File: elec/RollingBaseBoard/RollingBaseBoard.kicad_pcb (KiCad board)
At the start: 2 copper layers, 80 x 80 mm, 102 parts, among them P1 GP2, P10 UART_2, P11 I2C, P12 Motor, P13 Motor, P14 Encoder2, P15 Motor, P16 Switch, P17 Switch, P18 Switch, P19 Switch, P2 GP2, P20 Switch, P3 GP2, P4 GP2, P5 Bat5V, P6 Bat15V, P7 Encoder, P8 Encoder, P9 UART_1, U1 LMD18201, U2 LMD18201, U3 Teensy3.1

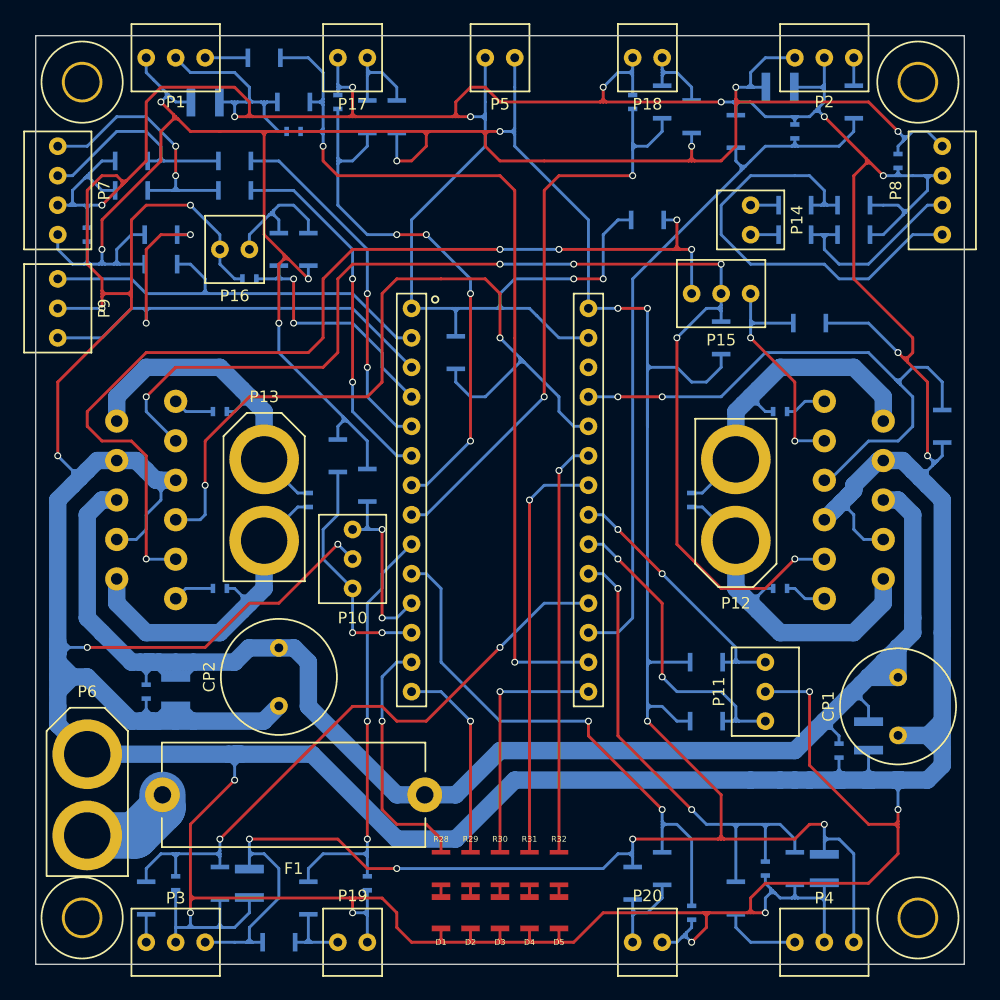
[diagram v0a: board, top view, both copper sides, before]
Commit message: Fixing rolling base board routing after footprints change.
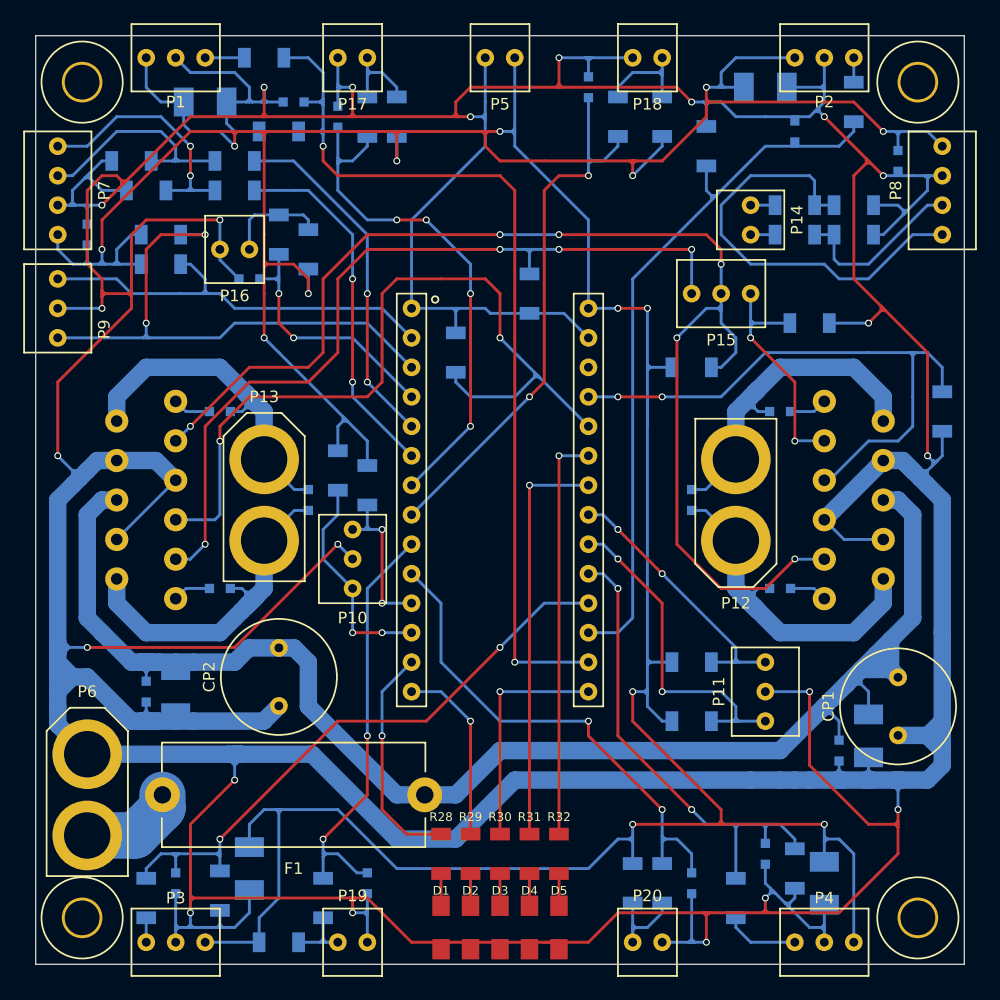
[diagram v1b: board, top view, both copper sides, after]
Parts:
- moved R26 12.0 mm to (151.0, 87.2), turned to 90 degrees
- moved R38 4.02 mm to (158.7, 72.0)
- moved C23 4.02 mm to (156.1, 69.4)
- moved R1 3.59 mm to (165.0, 93.6), turned to 180 degrees
- moved R3 2.84 mm to (129.4, 73.2)
- moved R5 2.84 mm to (166.3, 74.5)
- moved C2 2.54 mm to (130.7, 70.7)
- moved C25 2.54 mm to (165.0, 138.0)
- moved R37 2.54 mm to (162.5, 72.0)
- moved C22 1.27 mm to (134.5, 72.0)
- moved C5 1.27 mm to (126.9, 136.8)
- moved C7 1.27 mm to (176.4, 138.0)
- moved C8 1.27 mm to (171.4, 135.5)
- moved D1 1.27 mm to (143.4, 141.8)
- moved D2 1.27 mm to (146.0, 141.8)
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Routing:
- net /Com/GND: track 795.0 -> 745.9 mm, vias 24 -> 22
- net /Driver_2/Direction: track 87.9 -> 71.8 mm, vias 5 -> 4
- net /Driver_1/+15V: track 151.3 -> 137.2 mm
- net /Com/+5V: track 372.5 -> 378.7 mm, vias 16 -> 14
- net Net-(C18-Pad1): track 31.6 -> 35.7 mm
- net Net-(C18-Pad2): track 32.4 -> 36.5 mm
- net /Teensy/LimitSwitch2: track 52.2 -> 48.4 mm
- net /Teensy/LimitSwitch4: track 47.7 -> 43.8 mm
- net /Driver_1/ThermalFlag: track 106.5 -> 109.6 mm
- net Net-(P16-Pad2): track 11.9 -> 8.82 mm
- net Net-(C13-Pad1): track 31.6 -> 34.1 mm
- net /Teensy/LimitSwitch1: track 47.9 -> 45.5 mm
- net Net-(R28-Pad1): track 21.8 -> 19.7 mm
- net /Com/SDA: track 27.9 -> 29.8 mm
- net Net-(P18-Pad2): track 7.33 -> 9.27 mm
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
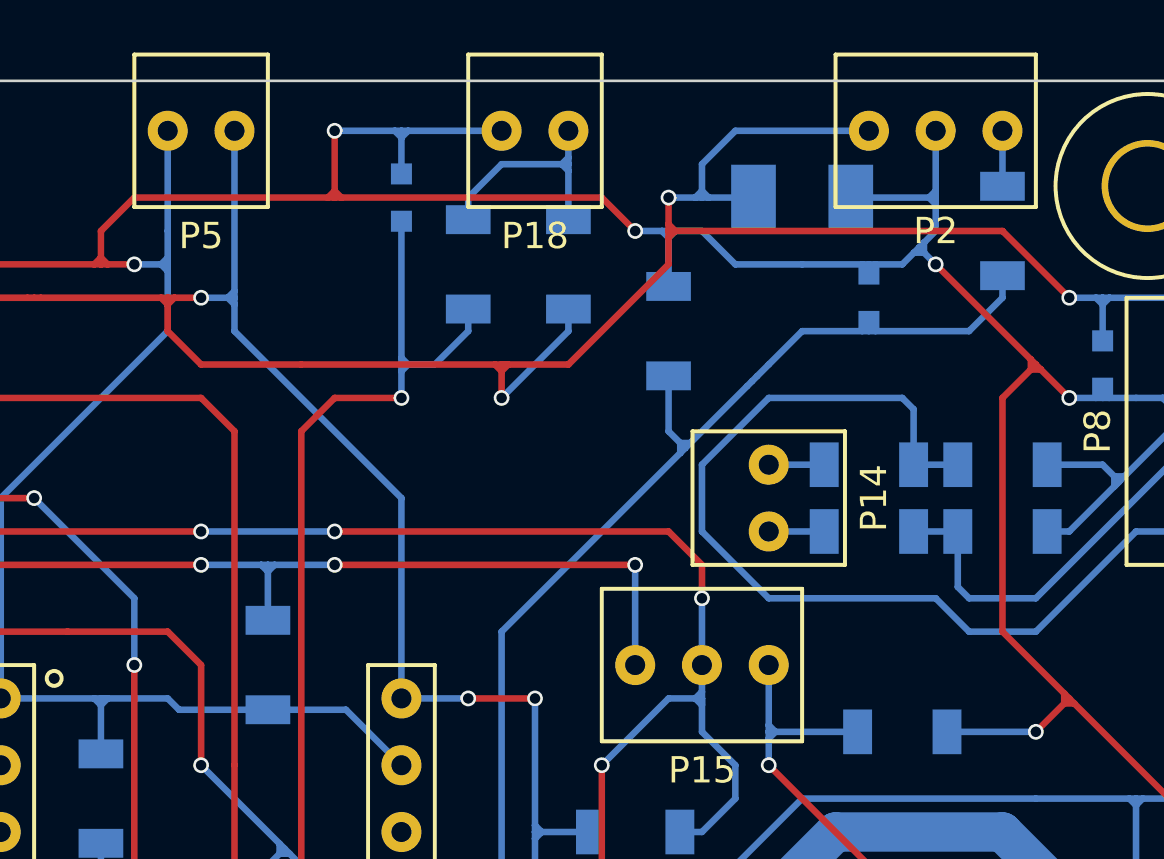
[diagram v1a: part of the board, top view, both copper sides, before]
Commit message: Optimising rolling base board routing a bit
Reduced via count by 6
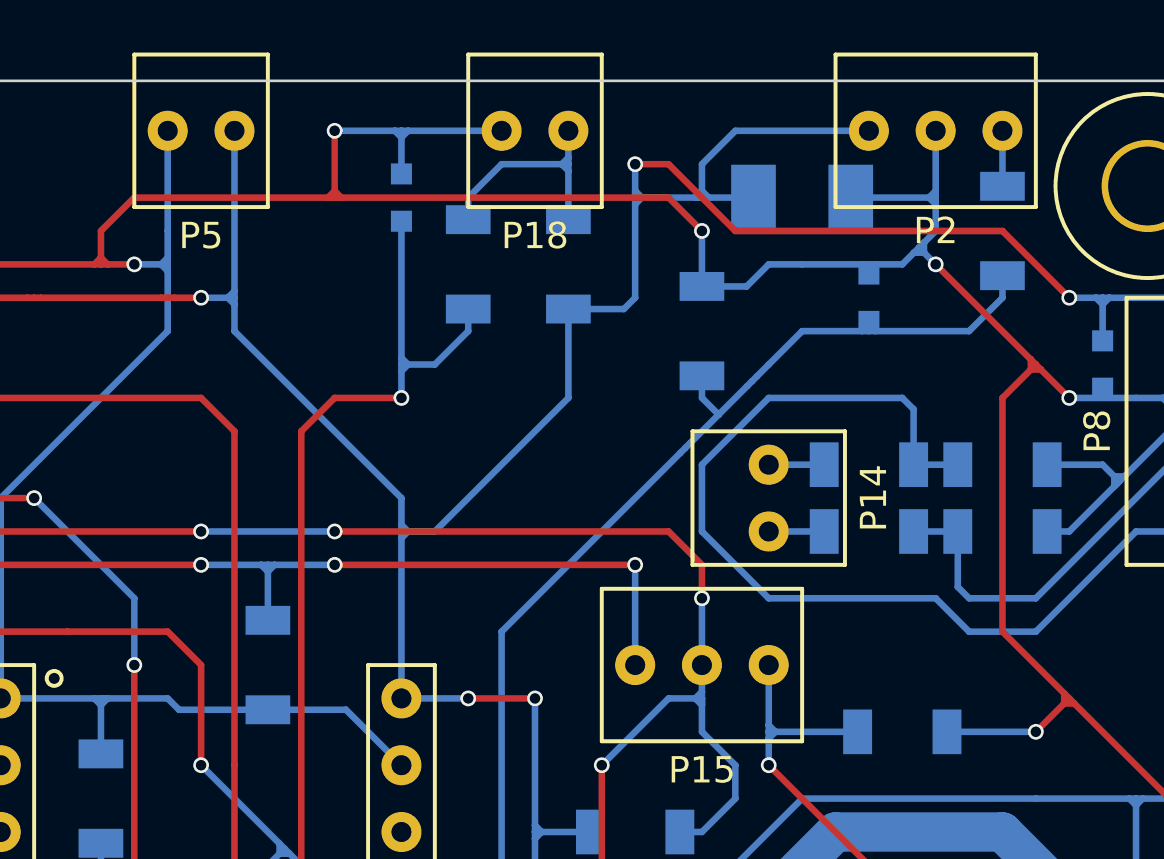
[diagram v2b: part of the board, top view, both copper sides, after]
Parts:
- moved R5 1.27 mm to (167.6, 74.5)
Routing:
- net /Com/+5V: track 378.7 -> 370.5 mm, vias 14 -> 13
- net /Teensy/GP2_2: track 62.5 -> 60.4 mm
- net /Com/GND: track 745.9 -> 744.7 mm

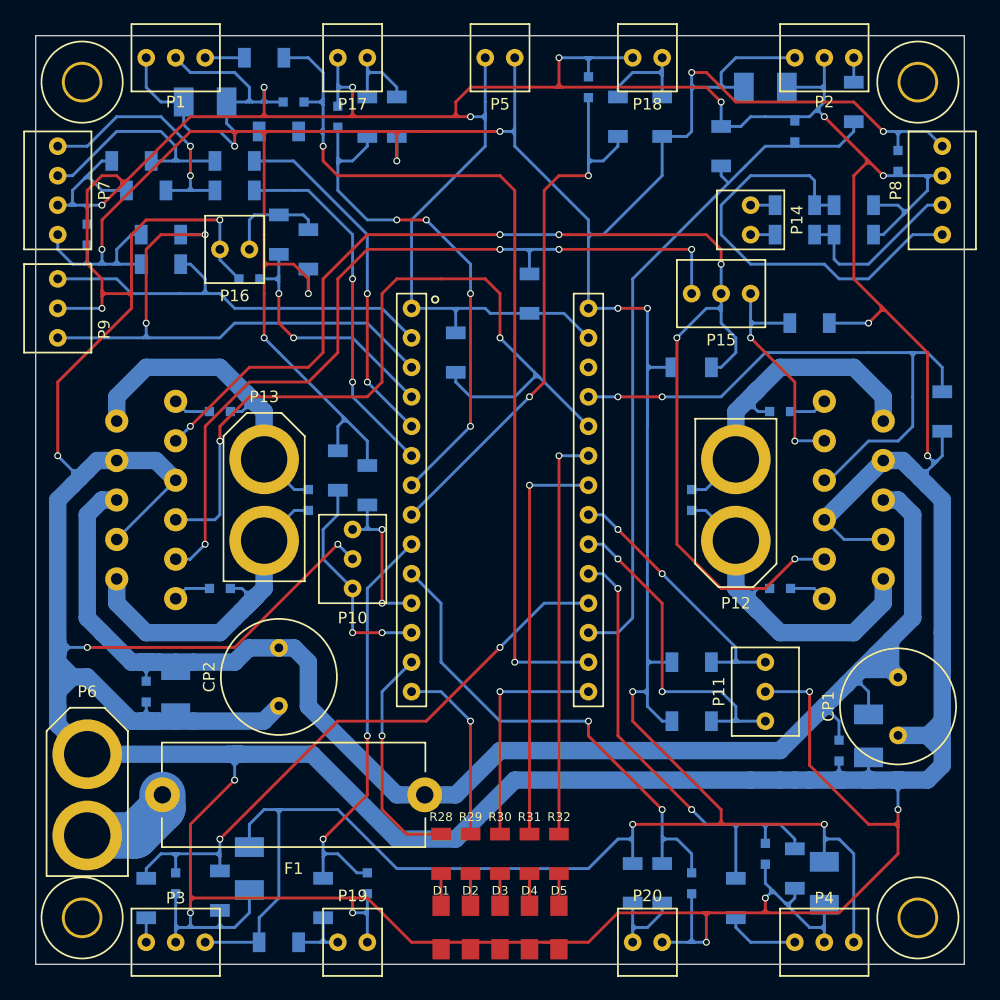
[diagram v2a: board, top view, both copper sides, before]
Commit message: Optimising rolling base board routing some more. Also removing a GND loop.
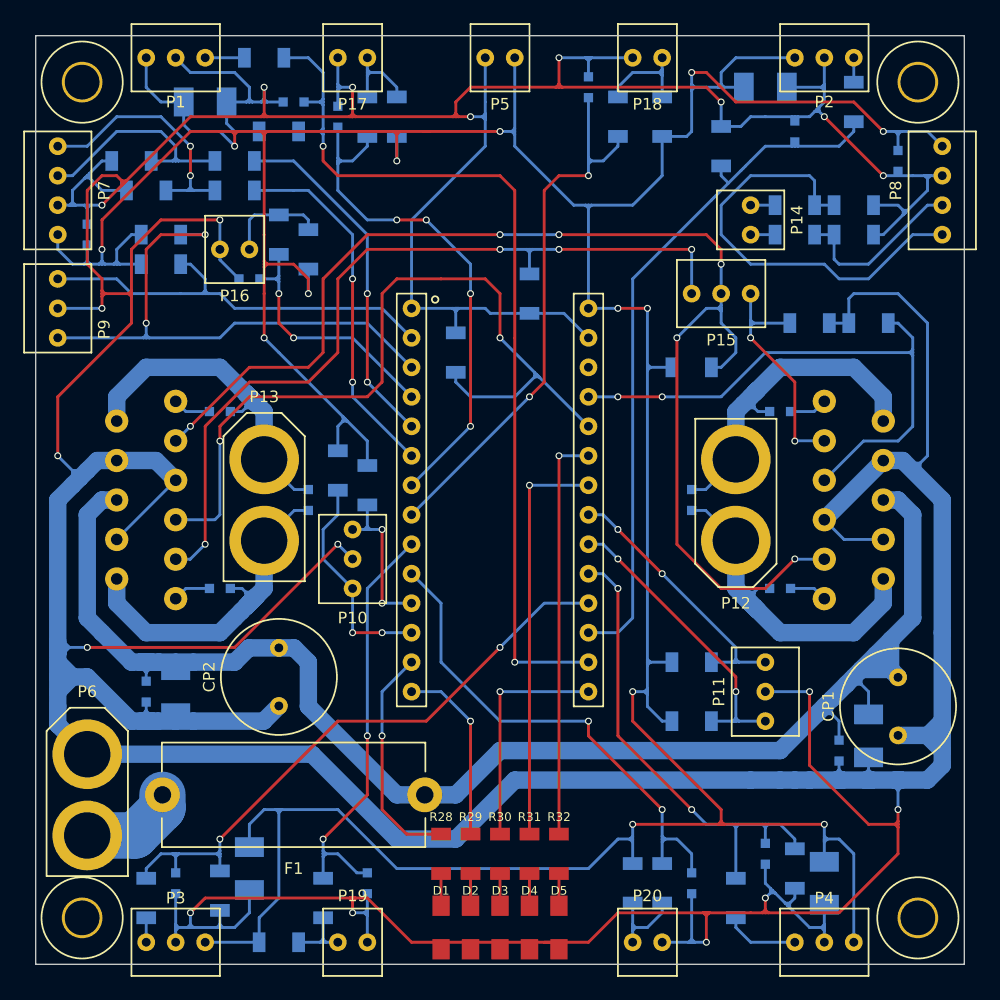
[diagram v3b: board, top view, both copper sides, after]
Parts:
- moved R25 9.92 mm to (180.2, 89.8), turned to 0 degrees
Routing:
- net /Com/GND: track 744.7 -> 708.7 mm, vias 22 -> 19
- net /Com/SDA: track 29.8 -> 27.1 mm
- net (no net): track 2.54 -> 0.00 mm
- net /Driver_1/PWM: track 51.3 -> 50.0 mm

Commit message: The rolling base board now has a name. Please welcome Hermes in the family.
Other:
- board text added: "Hermes board v1 Xenomorphales"
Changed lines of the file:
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@@
     (area 105.275 61.775 191.575 148.075)
     (thickness 1.6)
-    (drawings 4)
+    (drawings 5)
     (tracks 1367)
     (zones 0)
@@
       (net 2 /Com/+5V))
   )
+  (gr_text "Hermes board v1\n\nXenomorphales" (at 148.5 77.06) (layer F.SilkS)
+    (effects (font (size 1.5 1.5) (thickness 0.3)))
+  )
   (gr_line (start 108.5 145) (end 108.5 65) (angle 90) (layer Edge.Cuts) (width 0.1))

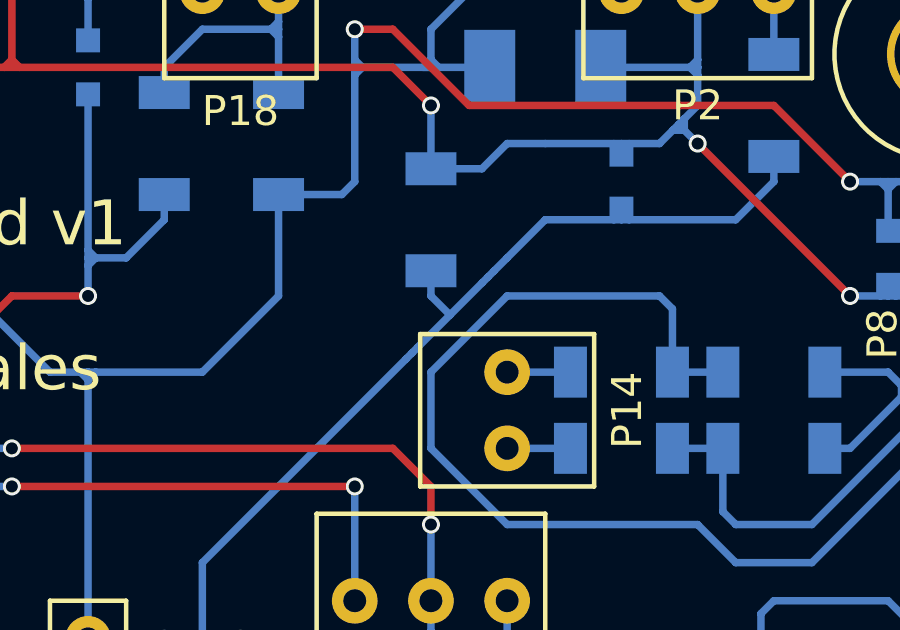
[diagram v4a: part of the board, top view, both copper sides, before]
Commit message: Minor fix to rolling base board routing
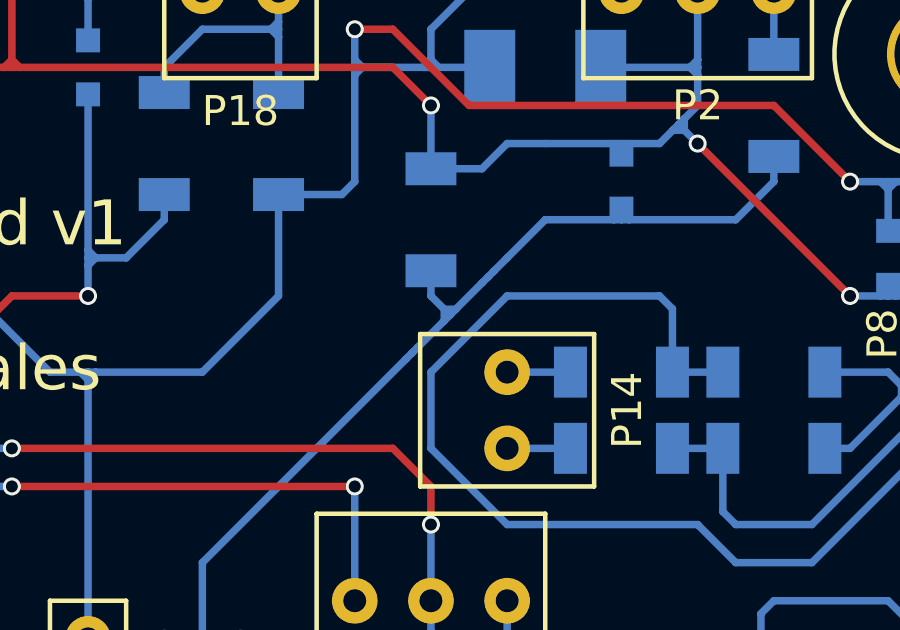
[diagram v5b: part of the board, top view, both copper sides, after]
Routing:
- net /Teensy/GP2_2: track 60.4 -> 61.2 mm
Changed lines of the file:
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@@
     (thickness 1.6)
     (drawings 5)
-    (tracks 1367)
+    (tracks 1372)
     (zones 0)
     (modules 102)
@@
   (segment (start 133.26 70.456) (end 133.26 70.71) (width 0.25) (layer B.Cu) (net 3))
   (segment (start 133.26 70.71) (end 133.26 70.964) (width 0.25) (layer B.Cu) (net 3))
+  (segment (start 167.9945 77.5045) (end 168.3755 77.5045) (width 0.25) (layer B.Cu) (net 4))
+  (segment (start 167.9945 77.5045) (end 167.9945 77.8855) (width 0.25) (layer B.Cu) (net 4))
   (segment (start 167.55 76.22) (end 167.55 77.06) (width 0.25) (layer B.Cu) (net 4))
-  (segment (start 167.55 77.06) (end 168.185 77.695) (width 0.25) (layer B.Cu) (net 4))
+  (segment (start 167.55 77.06) (end 167.9945 77.5045) (width 0.25) (layer B.Cu) (net 4))
+  (segment (start 167.9945 77.5045) (end 168.185 77.695) (width 0.25) (layer B.Cu) (net 4))
   (segment (start 178.98 72.41) (end 178.98 73.25) (width 0.25) (layer B.Cu) (net 4))
   (segment (start 177.71 74.52) (end 174.154 74.52) (width 0.25) (layer B.Cu) (net 4))
   (segment (start 178.98 73.25) (end 177.71 74.52) (width 0.25) (layer B.Cu) (net 4))
   (segment (start 169.455 76.425) (end 169.2645 76.6155) (width 0.25) (layer B.Cu) (net 4))
+  (segment (start 169.2645 76.6155) (end 168.3755 77.5045) (width 0.25) (layer B.Cu) (net 4))
+  (segment (start 169.455 76.425) (end 169.6455 76.2345) (width 0.25) (layer B.Cu) (net 4))
+  (segment (start 169.6455 76.2345) (end 170.09 75.79) (width 0.25) (layer B.Cu) (net 4))
+  (segment (start 171.36 74.52) (end 170.09 75.79) (width 0.25) (layer B.Cu) (net 4))
   (segment (start 171.36 74.52) (end 173.646 74.52) (width 0.25) (layer B.Cu) (net 4))
-  (segment (start 171.36 74.52) (end 170.09 75.79) (width 0.25) (layer B.Cu) (net 4))
-  (segment (start 169.6455 76.2345) (end 170.09 75.79) (width 0.25) (layer B.Cu) (net 4))
-  (segment (start 169.455 76.425) (end 169.6455 76.2345) (width 0.25) (layer B.Cu) (net 4))
-  (segment (start 169.2645 76.6155) (end 168.185 77.695) (width 0.25) (layer B.Cu) (net 4))
-  (segment (start 168.185 77.695) (end 167.1055 78.7745) (width 0.25) (layer B.Cu) (net 4))
+  (segment (start 168.3755 77.5045) (end 168.185 77.695) (width 0.25) (layer B.Cu) (net 4))
+  (segment (start 168.185 77.695) (end 167.9945 77.8855) (width 0.25) (layer B.Cu) (net 4))
+  (segment (start 167.9945 77.8855) (end 167.1055 78.7745) (width 0.25) (layer B.Cu) (net 4))
+  (segment (start 159.93 85.95) (end 159.93 115.16) (width 0.25) (layer B.Cu) (net 4))
+  (segment (start 159.93 115.16) (end 158.66 116.43) (width 0.25) (layer B.Cu) (net 4))
+  (segment (start 158.66 116.43) (end 156.12 116.43) (width 0.25) (layer B.Cu) (net 4))
+  (segment (start 166.7245 79.1555) (end 159.93 85.95) (width 0.25) (layer B.Cu) (net 4))
+  (segment (start 166.915 78.965) (end 166.7245 79.1555) (width 0.25) (layer B.Cu) (net 4))
   (segment (start 167.1055 78.7745) (end 166.915 78.965) (width 0.25) (layer B.Cu) (net 4))
-  (segment (start 166.915 78.965) (end 166.7245 79.1555) (width 0.25) (layer B.Cu) (net 4))
-  (segment (start 166.7245 79.1555) (end 159.93 85.95) (width 0.25) (layer B.Cu) (net 4))
-  (segment (start 158.66 116.43) (end 156.12 116.43) (width 0.25) (layer B.Cu) (net 4))
-  (segment (start 159.93 115.16) (end 158.66 116.43) (width 0.25) (layer B.Cu) (net 4))
-  (segment (start 159.93 85.95) (end 159.93 115.16) (width 0.25) (layer B.Cu) (net 4))
   (segment (start 174.154 74.52) (end 173.9 74.52) (width 0.25) (layer B.Cu) (net 4))
   (segment (start 173.646 74.52) (end 173.9 74.52) (width 0.25) (layer B.Cu) (net 4))
